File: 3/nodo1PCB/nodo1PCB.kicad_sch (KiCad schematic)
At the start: 18 parts, among them J2 I2C, J3 Analog, J6 Analog, J7 Digital, K1 G3MB-202P

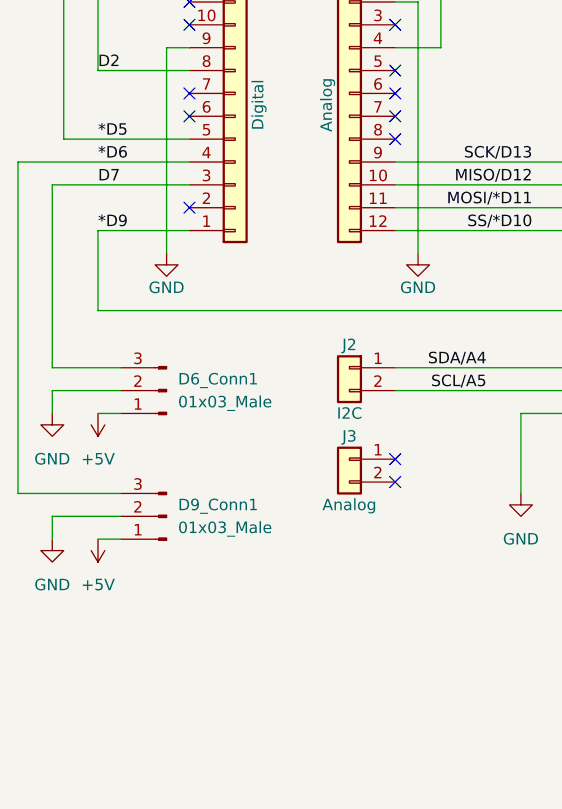
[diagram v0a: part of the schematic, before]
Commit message: Acabar layout alimentación PCB
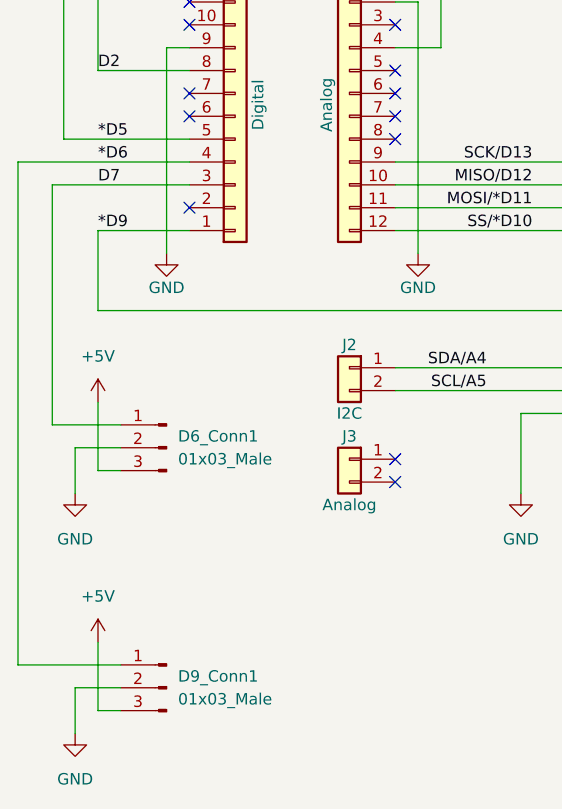
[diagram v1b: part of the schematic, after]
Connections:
- net *D6: now also D9_Conn1.1 (Pin_1); no longer D9_Conn1.3 (Pin_3)
- net +5V: now also D6_Conn1.3 (Pin_3), D9_Conn1.3 (Pin_3); no longer D6_Conn1.1 (Pin_1), D9_Conn1.1 (Pin_1)
- net D7: now also D6_Conn1.1 (Pin_1); no longer D6_Conn1.3 (Pin_3)
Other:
- moved on the sheet: D6_Conn1, D9_Conn1

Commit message: Terminar PCB
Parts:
- removed J3: Analog, Connector_PinHeader_2.54mm:PinHeader_1x02_P2.54mm_Vertical, symbol Connector_Generic:Conn_01x02
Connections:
- net SCL/A5: now also J2.1 (Pin_1); no longer J2.2 (Pin_2)
- net SDA/A4: now also J2.2 (Pin_2); no longer J2.1 (Pin_1)
- no-connect marks 13 -> 11
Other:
- moved on the sheet: BJT1, D6_Conn1, D9_Conn1, F1, F2, F3, I2C_Conn1, J2, J6, J7, K1, PS1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
